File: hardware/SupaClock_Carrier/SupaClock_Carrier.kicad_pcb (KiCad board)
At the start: 2 copper layers, 85 x 67 mm, 25 parts, among them J11 AD8232_SparkFun, J12_LA1 ECG_LA_pad_M3, J12_RA1 ECG_RA_pad_M3, J12_RL1 ECG_RL_pad_M3, J13 AD8232_Pads_RA_LA_RL, J14 MAX30102_bot, J15 XIAO_BAT_Wires, J3 MAX30102_top, J4 MAX30205_8pad, J5 BMI160_7p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

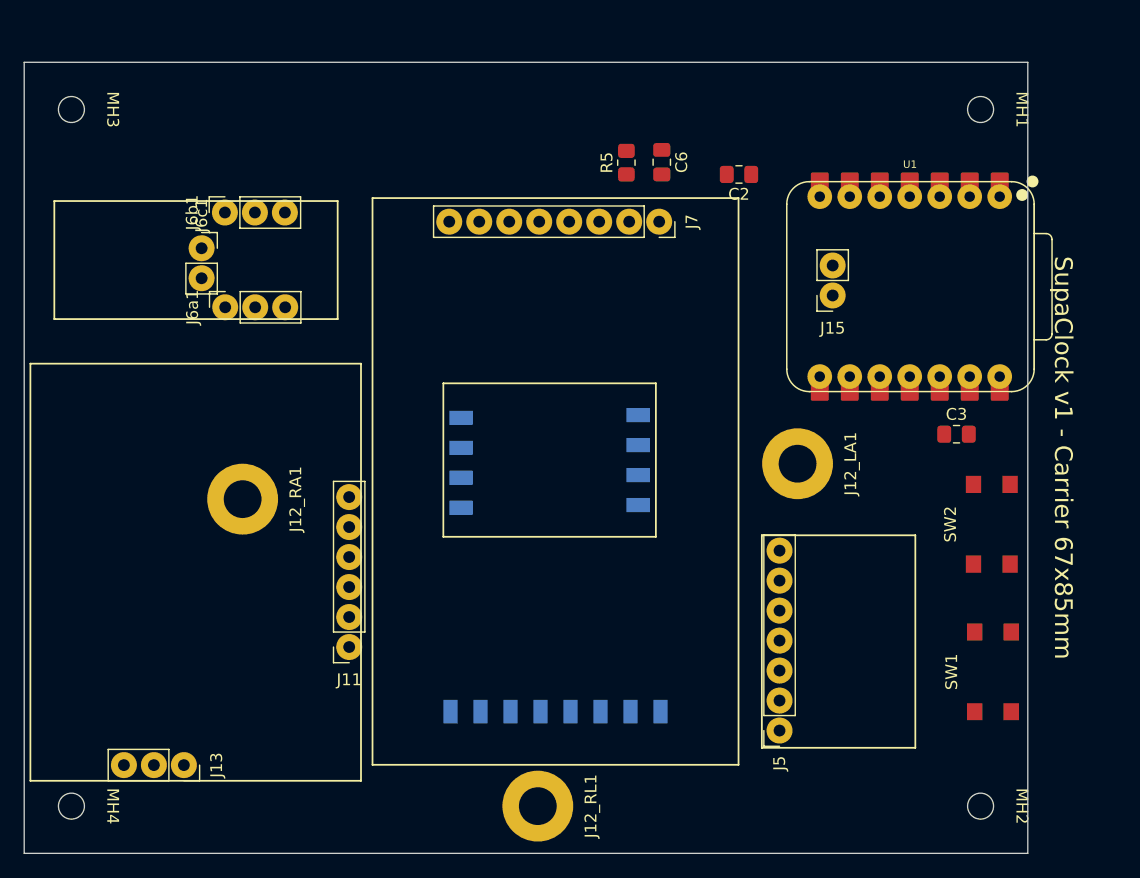
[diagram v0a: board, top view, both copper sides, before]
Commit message: Update design rule severities in SupaClock_Carrier project
- Changed clearance rule severity from error to ignore
- Changed nonmirrored text on back layer rule severity from warning to ignore
- Updated silk over copper and silk overlap rule severities from warning to ignore
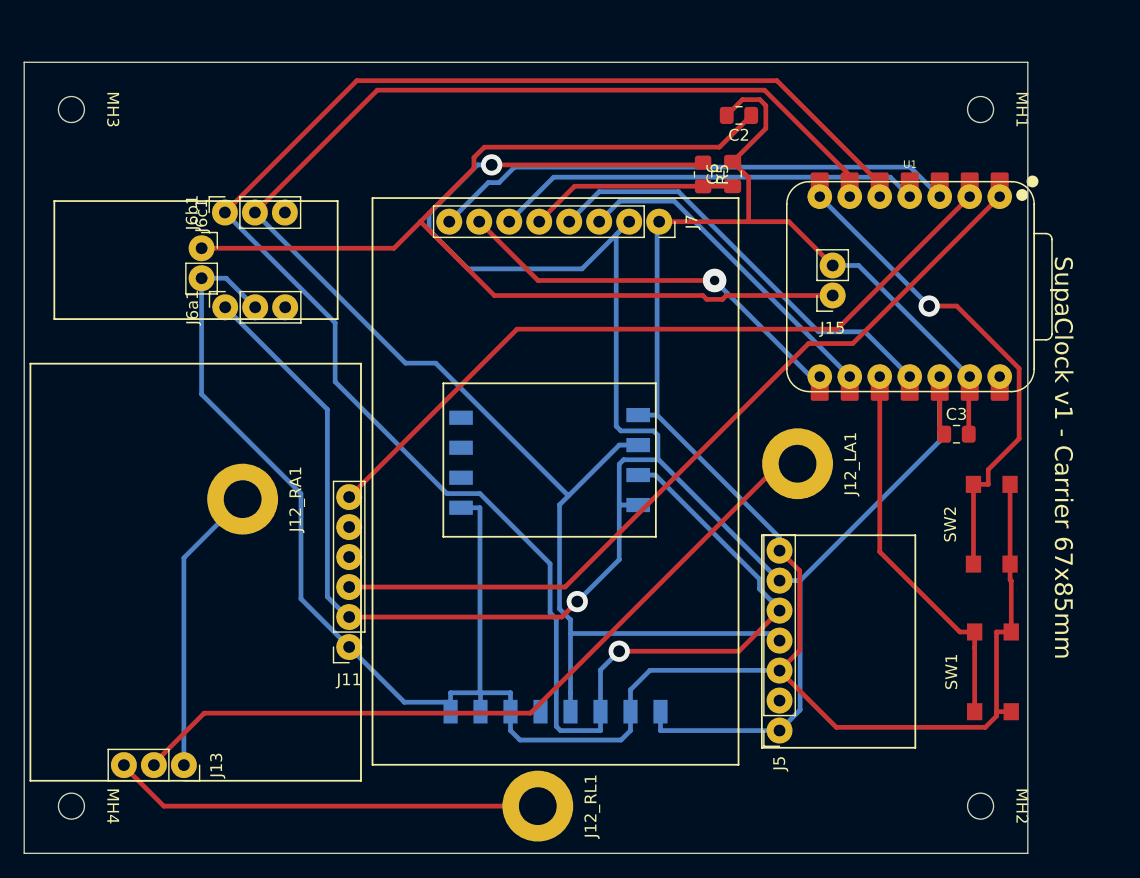
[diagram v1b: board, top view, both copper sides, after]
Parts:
- moved R5 6.58 mm to (119.0, 33.0), turned to -90 degrees
- moved C6 6.08 mm to (121.5, 33.0), turned to 90 degrees
- moved C2 5.00 mm to (122.0, 28.0)
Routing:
- net /GND: track 0.00 -> 249.5 mm
- net /+3V3: track 0.00 -> 207.7 mm, vias 0 -> 2
- net /I2C_SDA: track 0.00 -> 165.6 mm, vias 0 -> 1
- net /I2C_SCL: track 0.00 -> 140.6 mm
- net /+BATT: track 0.00 -> 89.5 mm
- net /ECG_OUT: track 0.00 -> 69.6 mm
- net /ECG_LA: track 0.00 -> 65.2 mm
- net /ECG_SDN: track 0.00 -> 63.9 mm
- net /BLK_PWM: track 0.00 -> 45.3 mm
- net /BTN_NEXT: track 0.00 -> 42.7 mm, vias 0 -> 1
- net /SPI_MOSI: track 0.00 -> 37.2 mm
- net /SPI_DC: track 0.00 -> 37.0 mm
- net /ECG_RL: track 0.00 -> 36.6 mm
- net /SPI_CS: track 0.00 -> 35.1 mm, vias 0 -> 1
- net /BTN_SELECT: track 0.00 -> 32.4 mm
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
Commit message: Update design rules and footprint for MAX30102
- Increased minimum through hole diameter from 0.8mm to 1.0mm.
- Adjusted minimum via annular width from 0.6mm to 0.4mm and minimum via diameter from 2.0mm to 1.8mm.
- Modified the footprint for MAX30102_Castellated_1x4 by changing the yard dimensions and adding additional lines for improved clarity.
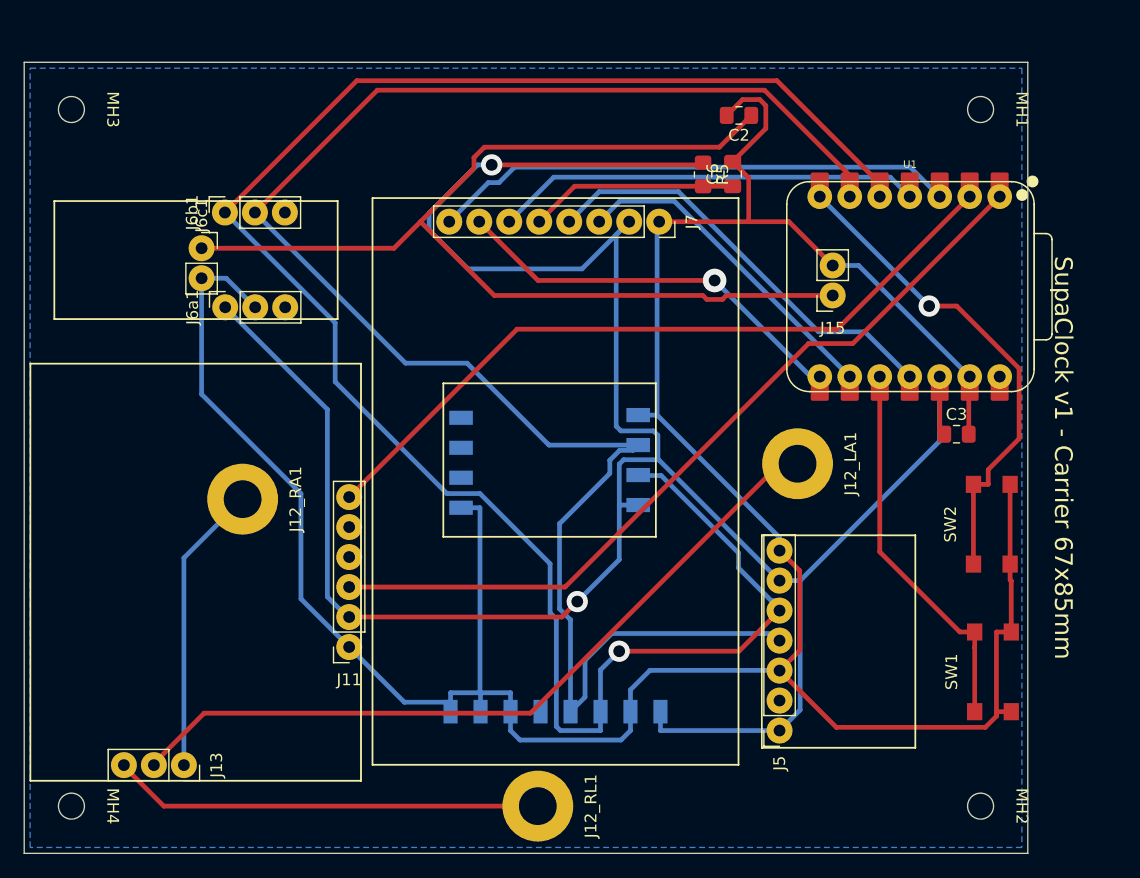
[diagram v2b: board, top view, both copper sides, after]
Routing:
- net /I2C_SCL: track 140.6 -> 149.0 mm
- added copper zone on B.Cu, net /GND

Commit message: Add DRC JSON files for SupaClock Carrier: drc_post_relax.json and drc_post_thtswap.json
- Created drc_post_relax.json with 509 violations and warnings related to thermal relief, text dimensions, and footprint mismatches.
- Created drc_post_thtswap.json with 653 violations and warnings, including unconnected items, hole size issues, and silkscreen clearance violations.
- Both files include ignored checks and are formatted according to the KiCad DRC schema.
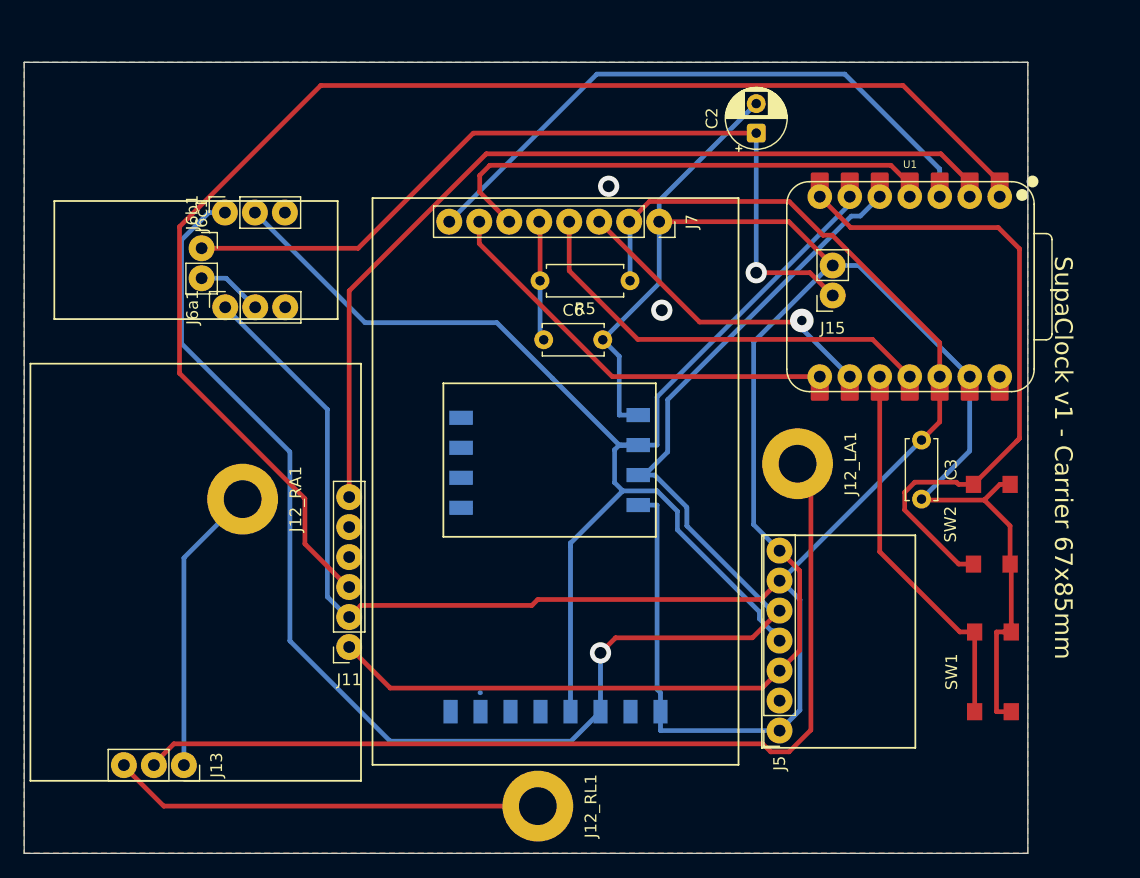
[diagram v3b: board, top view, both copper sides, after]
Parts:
- removed MH1, MH2, MH3, MH4: M2_Mount, MountingHole:MountingHole_2.2mm_M2
- C2: footprint Capacitor_SMD:C_0805_2012Metric_Pad1.18x1.45mm_HandSolder -> Capacitor_THT:CP_Radial_D5.0mm_P2.50mm
- C3, C6: footprint Capacitor_SMD:C_0805_2012Metric_Pad1.18x1.45mm_HandSolder -> Capacitor_THT:C_Disc_D5.0mm_W2.5mm_P5.00mm
- R5: footprint Resistor_SMD:R_0805_2012Metric_Pad1.20x1.40mm_HandSolder -> Resistor_THT:R_Axial_DIN0207_L6.3mm_D2.5mm_P7.62mm_Horizontal
- moved C6 21.3 mm to (105.5, 47.0), turned to 0 degrees
- moved R5 10.9 mm to (112.8, 42.0), turned to 180 degrees
- moved C3 3.00 mm to (137.5, 55.5), turned to -90 degrees
- moved C2 2.09 mm to (123.5, 29.5), turned to 90 degrees
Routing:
- net /GND: track 249.5 -> 193.5 mm, vias 0 -> 2
- net /ECG_OUT: track 69.6 -> 115.6 mm
- net /+3V3: track 207.7 -> 176.2 mm, vias 2 -> 0
- net /I2C_SCL: track 149.0 -> 118.0 mm
- net /+BATT: track 89.5 -> 70.1 mm, vias 0 -> 1
- net /I2C_SDA: track 165.8 -> 147.6 mm
- net /ECG_LA: track 65.2 -> 80.5 mm
- net /BTN_NEXT: track 42.7 -> 56.9 mm, vias 1 -> 0
- net /ECG_SDN: track 63.9 -> 77.0 mm
- net /BLK_PWM: track 45.3 -> 53.2 mm
- net /SPI_RES: track 17.6 -> 10.2 mm
- net /SPI_DC: track 37.0 -> 43.5 mm
- net /SPI_CS: track 35.1 -> 36.2 mm, vias 1 -> 0
- net /SPI_SCK: track 28.9 -> 28.0 mm, vias 0 -> 1
- added copper zone on F.Cu, net /GND

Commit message: Add DRC configuration file for SupaClock Carrier with detailed violation reports
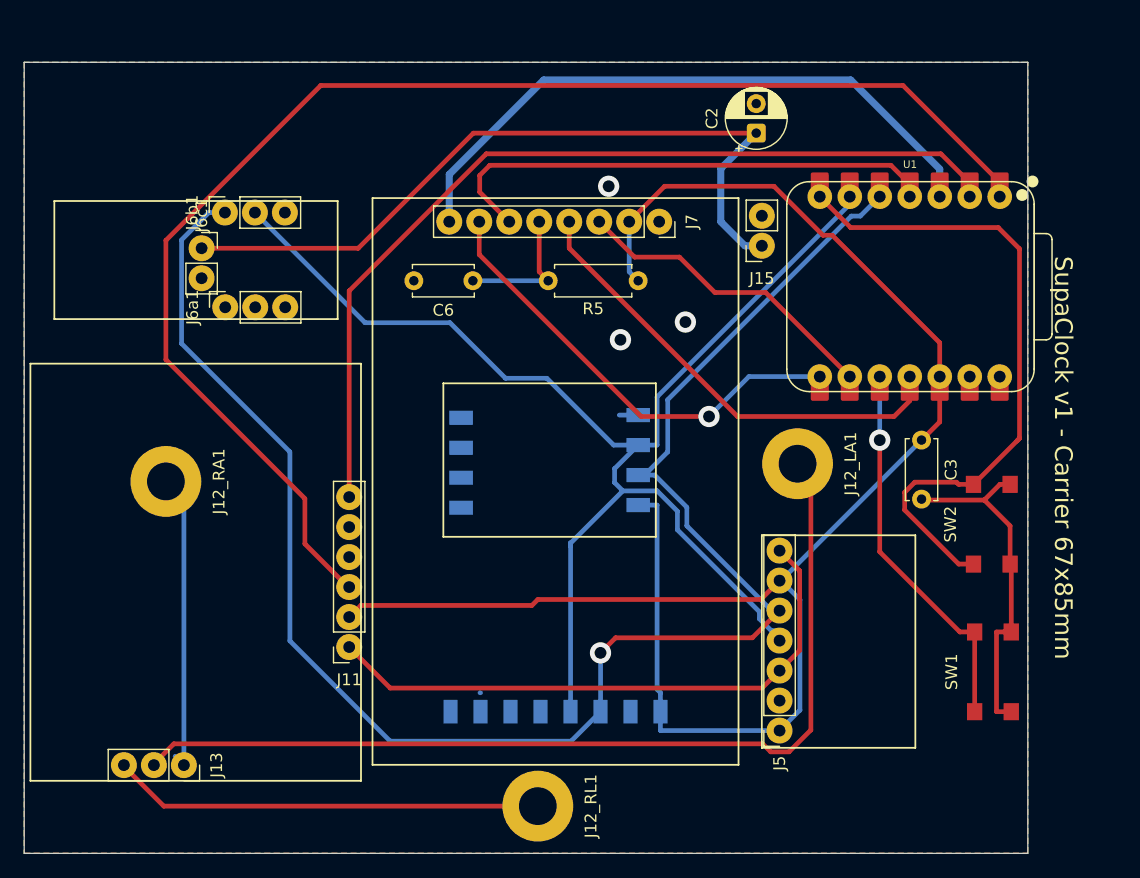
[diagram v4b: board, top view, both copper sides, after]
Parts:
- moved C6 7.81 mm to (99.5, 42.0), turned to 180 degrees
- moved J15 7.33 mm to (124.0, 39.0)
- moved J12_RA1 6.67 mm to (73.5, 59.0)
- moved R5 0.69 mm to (113.5, 42.0)
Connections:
- J6a1 pad 1: /+3V3 -> unconnected-(J6a1-Pin_1-Pad1)
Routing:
- net /GND: track 193.5 -> 83.9 mm, vias 2 -> 3
- net /+3V3: track 176.2 -> 147.1 mm
- net /+BATT: track 70.1 -> 64.1 mm, vias 1 -> 0
- net /SPI_CS: track 36.2 -> 39.5 mm, vias 0 -> 1
- net /ECG_RA: track 24.6 -> 27.5 mm
- net /SPI_RES: track 10.2 -> 12.5 mm
- net /SPI_MOSI: track 37.5 -> 39.6 mm
- net /BLK_PWM: track 53.2 -> 55.2 mm
- net /ECG_OUT: track 115.6 -> 116.5 mm
- net /I2C_SCL: track 118.0 -> 117.1 mm
- net /BTN_SELECT: track 32.4 -> 33.3 mm, vias 0 -> 1
- net /SPI_SCK: track 28.0 -> 27.5 mm, vias 1 -> 0

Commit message: feat(mechanical): add SupaClock V2 concept design with enhanced aesthetics
- Introduced `supaclock_v2_concept.scad` for visual representation of the new design.
- Added `supaclock_v2_dimensions.md` detailing critical dimensions for Fusion 360 reconstruction.
- Created `supaclock_v2_top_case.scad` for the functional top case with improved features.
- Generated corresponding STL files for both concept and top case.
- Updated partitioning for ESP32-C3 SuperMini in `partitions_c3.csv`.
- Migration to ESP32 S3
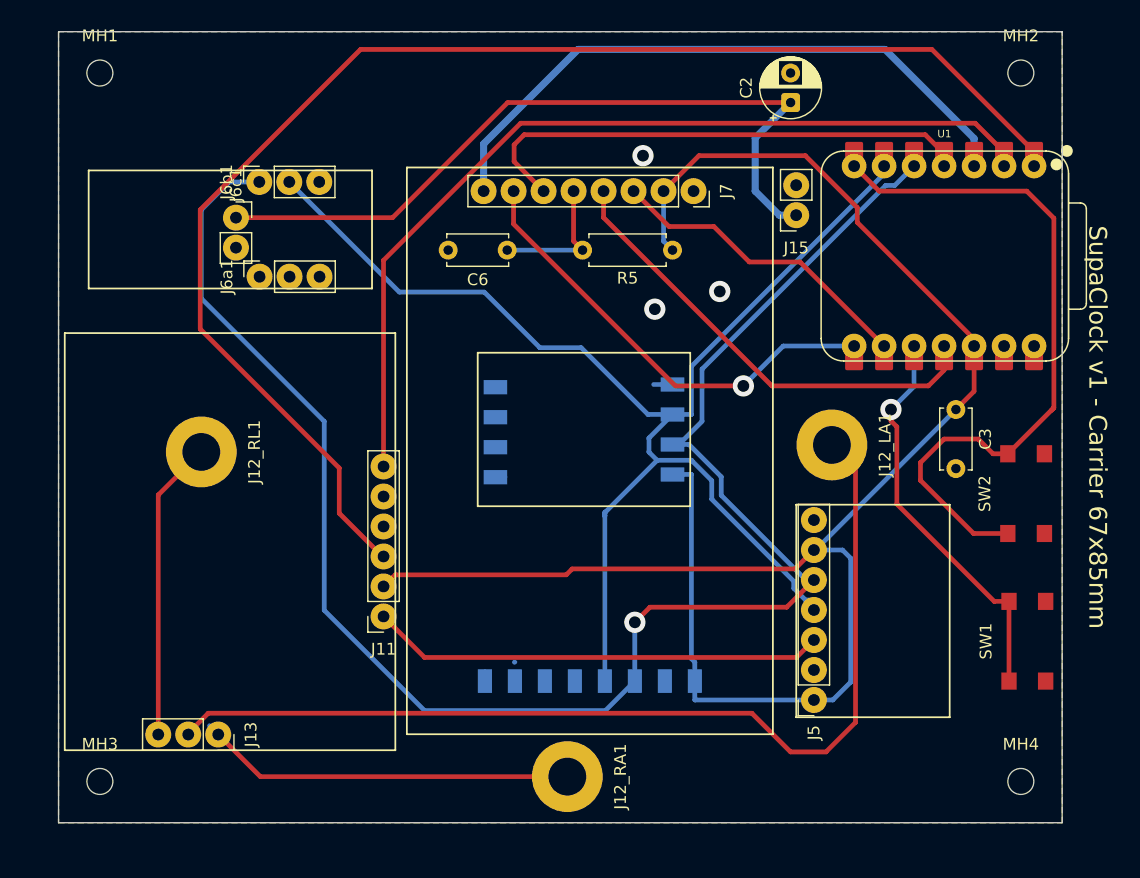
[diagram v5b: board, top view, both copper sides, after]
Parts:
- added MH1: MountingHole_2.2mm_M2, MountingHole:MountingHole_2.2mm_M2, F.Cu at (67.9, 24.4)
- added MH2: MountingHole_2.2mm_M2, MountingHole:MountingHole_2.2mm_M2, F.Cu at (145.9, 24.4)
- added MH3: MountingHole_2.2mm_M2, MountingHole:MountingHole_2.2mm_M2, F.Cu at (67.9, 84.4)
- added MH4: MountingHole_2.2mm_M2, MountingHole:MountingHole_2.2mm_M2, F.Cu at (145.9, 84.4)
- moved J12_RA1 42.2 mm to (107.5, 84.0)
- moved J12_RL1 41.4 mm to (76.5, 56.5)
- moved SW2 3.90 mm to (146.4, 60.0)
- moved J5 3.90 mm to (128.4, 77.5)
- moved C6 3.90 mm to (102.4, 39.4)
- moved J3 3.90 mm to (102.4, 54.8)
- moved J6b1 3.90 mm to (81.4, 33.6)
- moved J7 3.90 mm to (118.2, 34.4)
- moved R5 3.90 mm to (116.4, 39.4)
- moved C2 3.90 mm to (126.4, 26.9)
- moved J14 3.90 mm to (117.4, 54.6)
- moved J15 3.90 mm to (126.9, 36.4)
- moved J4 3.90 mm to (109.4, 70.9)
- moved J11 3.90 mm to (91.9, 70.4)
- moved J13 3.90 mm to (77.9, 80.4)
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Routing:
- net /GND: track 83.9 -> 42.8 mm
- net /ECG_RL: track 36.6 -> 25.5 mm
- net /ECG_LA: track 80.5 -> 85.0 mm
- net /BTN_NEXT: track 56.9 -> 60.9 mm
- net /ECG_RA: track 27.5 -> 31.0 mm
- net /+3V3: track 147.1 -> 150.0 mm
- net /I2C_SDA: track 147.6 -> 149.3 mm
- net /BTN_SELECT: track 33.3 -> 34.9 mm

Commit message: nurvos cambios
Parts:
- added C4: 100nF, Capacitor_THT:C_Disc_D5.0mm_W2.5mm_P5.00mm, F.Cu at (112.5, 46.0)
- added C5: 100nF, Capacitor_THT:C_Disc_D5.0mm_W2.5mm_P5.00mm, F.Cu at (107.5, 25.0)
- added R1: 4.7k, Resistor_THT:R_Axial_DIN0207_L6.3mm_D2.5mm_P7.62mm_Horizontal, F.Cu at (88.3, 66.5)
- added R2: 4.7k, Resistor_THT:R_Axial_DIN0207_L6.3mm_D2.5mm_P7.62mm_Horizontal, F.Cu at (94.0, 32.7)
- added R3: 10k, Resistor_THT:R_Axial_DIN0207_L6.3mm_D2.5mm_P7.62mm_Horizontal, F.Cu at (104.7, 42.5)
- added R4: 10k, Resistor_THT:R_Axial_DIN0207_L6.3mm_D2.5mm_P7.62mm_Horizontal, F.Cu at (90.9, 26.5)
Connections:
- J7 pad 1: /GND -> /BLK_PWM
- J7 pad 2: /+3V3 -> /SPI_CS
- J7 pad 3: /SPI_SCK -> /SPI_DC
- J7 pad 4: /SPI_MOSI -> /SPI_RES
- J7 pad 5: /SPI_RES -> /SPI_MOSI
- J7 pad 6: /SPI_DC -> /SPI_SCK
- J7 pad 7: /SPI_CS -> /+3V3
- J7 pad 8: /BLK_PWM -> /GND
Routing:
- net /BTN_NEXT: track 60.9 -> 138.0 mm
- net /+3V3: track 150.0 -> 224.1 mm
- net /BTN_SELECT: track 34.9 -> 63.8 mm
- net /BLK_PWM: track 55.2 -> 36.7 mm
- net /SPI_SCK: track 27.5 -> 45.7 mm, vias 0 -> 1
- net /SPI_CS: track 39.5 -> 22.5 mm, vias 1 -> 0
- net /SPI_DC: track 43.5 -> 30.0 mm
- net /I2C_SCL: track 117.1 -> 119.9 mm
- net /SPI_MOSI: track 39.6 -> 42.2 mm

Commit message: ultimos cambios
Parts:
- removed C4, C5: 100nF, Capacitor_THT:C_Disc_D5.0mm_W2.5mm_P5.00mm
- removed R1, R2: 4.7k, Resistor_THT:R_Axial_DIN0207_L6.3mm_D2.5mm_P7.62mm_Horizontal
- removed R3, R4: 10k, Resistor_THT:R_Axial_DIN0207_L6.3mm_D2.5mm_P7.62mm_Horizontal
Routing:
- net /BTN_NEXT: track 138.0 -> 60.9 mm
- net /BTN_SELECT: track 63.8 -> 34.9 mm
- net /+3V3: track 224.1 -> 205.5 mm
- net /GND: vias 3 -> 1
